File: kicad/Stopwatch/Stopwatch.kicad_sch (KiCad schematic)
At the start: 8 parts

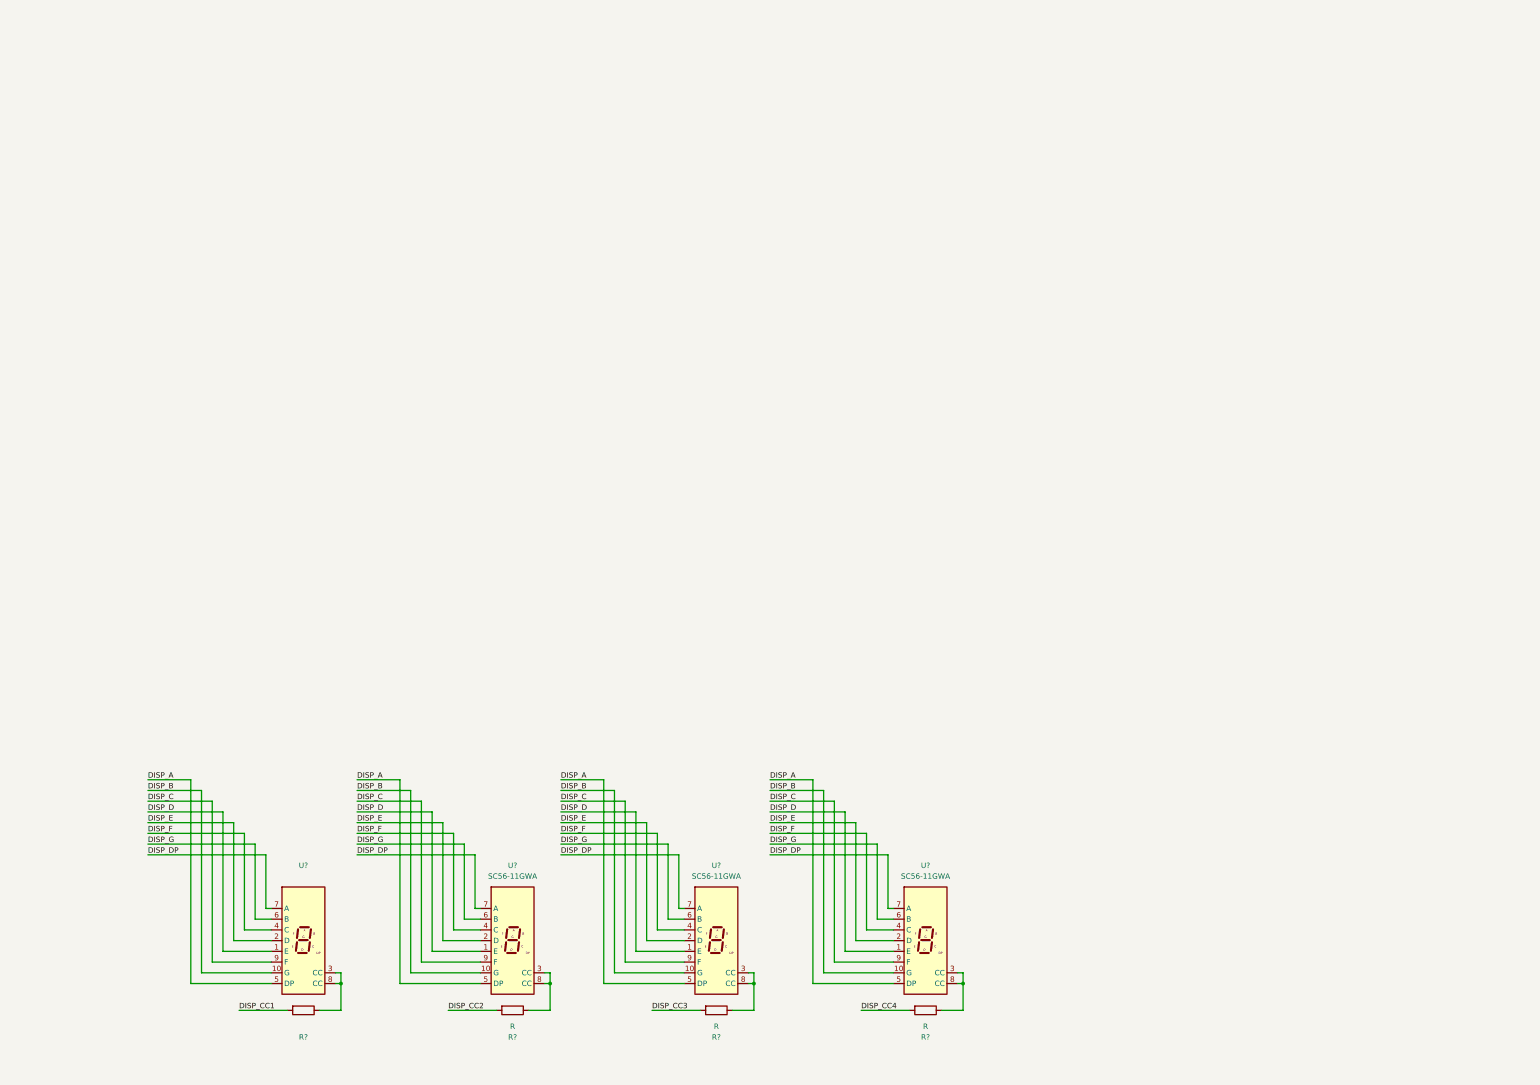
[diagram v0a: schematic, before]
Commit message: added BluePill to symbol library, completed first draft of Stopwatch schematic
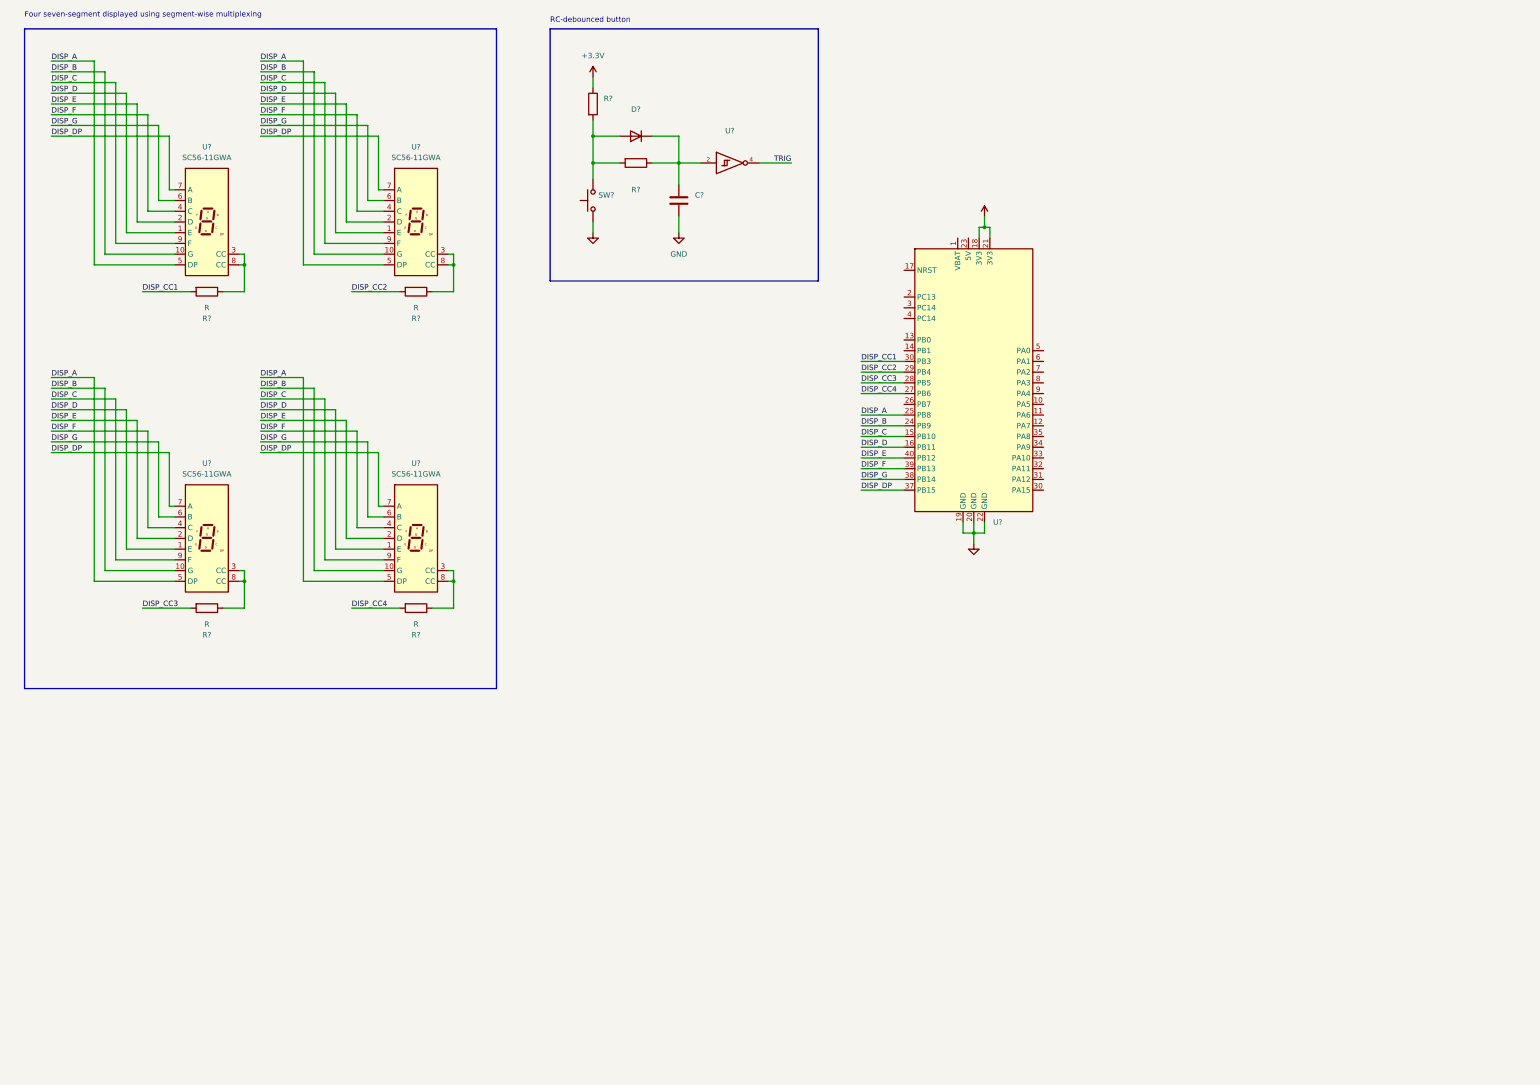
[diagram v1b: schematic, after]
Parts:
- added C?: (no value), symbol Device:C
- added D?: (no value), symbol Diode:1N4148
- added R? (x2): (no value), symbol Device:R
- added SW?: (no value), symbol Switch:SW_Push
- added U?: (no value), symbol 74xGxx:74AHCT1G14
- added U?: (no value), symbol Custom:BluePill
- R?: value (none) -> R
- U?: value (none) -> SC56-11GWA
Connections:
- net DISP_A: now also U?.25 (PB8)
- net DISP_B: now also U?.24 (PB9)
- net DISP_C: now also U?.15 (PB10)
- net DISP_CC1: now also U?.30 (PB3)
- net DISP_CC2: now also U?.29 (PB4)
- net DISP_CC3: now also U?.28 (PB5)
- net DISP_CC4: now also U?.27 (PB6)
- net DISP_D: now also U?.16 (PB11)
- net DISP_DP: now also U?.37 (PB15)
- net DISP_E: now also U?.40 (PB12)
- net DISP_F: now also U?.39 (PB13)
- net DISP_G: now also U?.38 (PB14)
- new net: C?.1, D?.1 (K), R?.1, U?.2
- new net: D?.2 (A), R?.2, R?.2, SW?.2
- new net +3V3: R?.1, U?.18 (3V3), U?.21 (3V3)
- new net GND: C?.2, SW?.1, U?.19 (GND), U?.20 (GND), U?.22 (GND), U?.3 (GND)
- new net TRIG: U?.4
- new net VCC: U?.5 (VCC)
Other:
- note added: "Four seven-segment displayed using segment-wise multiplexing"
- note added: "RC-debounced button"
- moved on the sheet: R?, U?

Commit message: updated Stopwatch with calculation for debouncer circuit
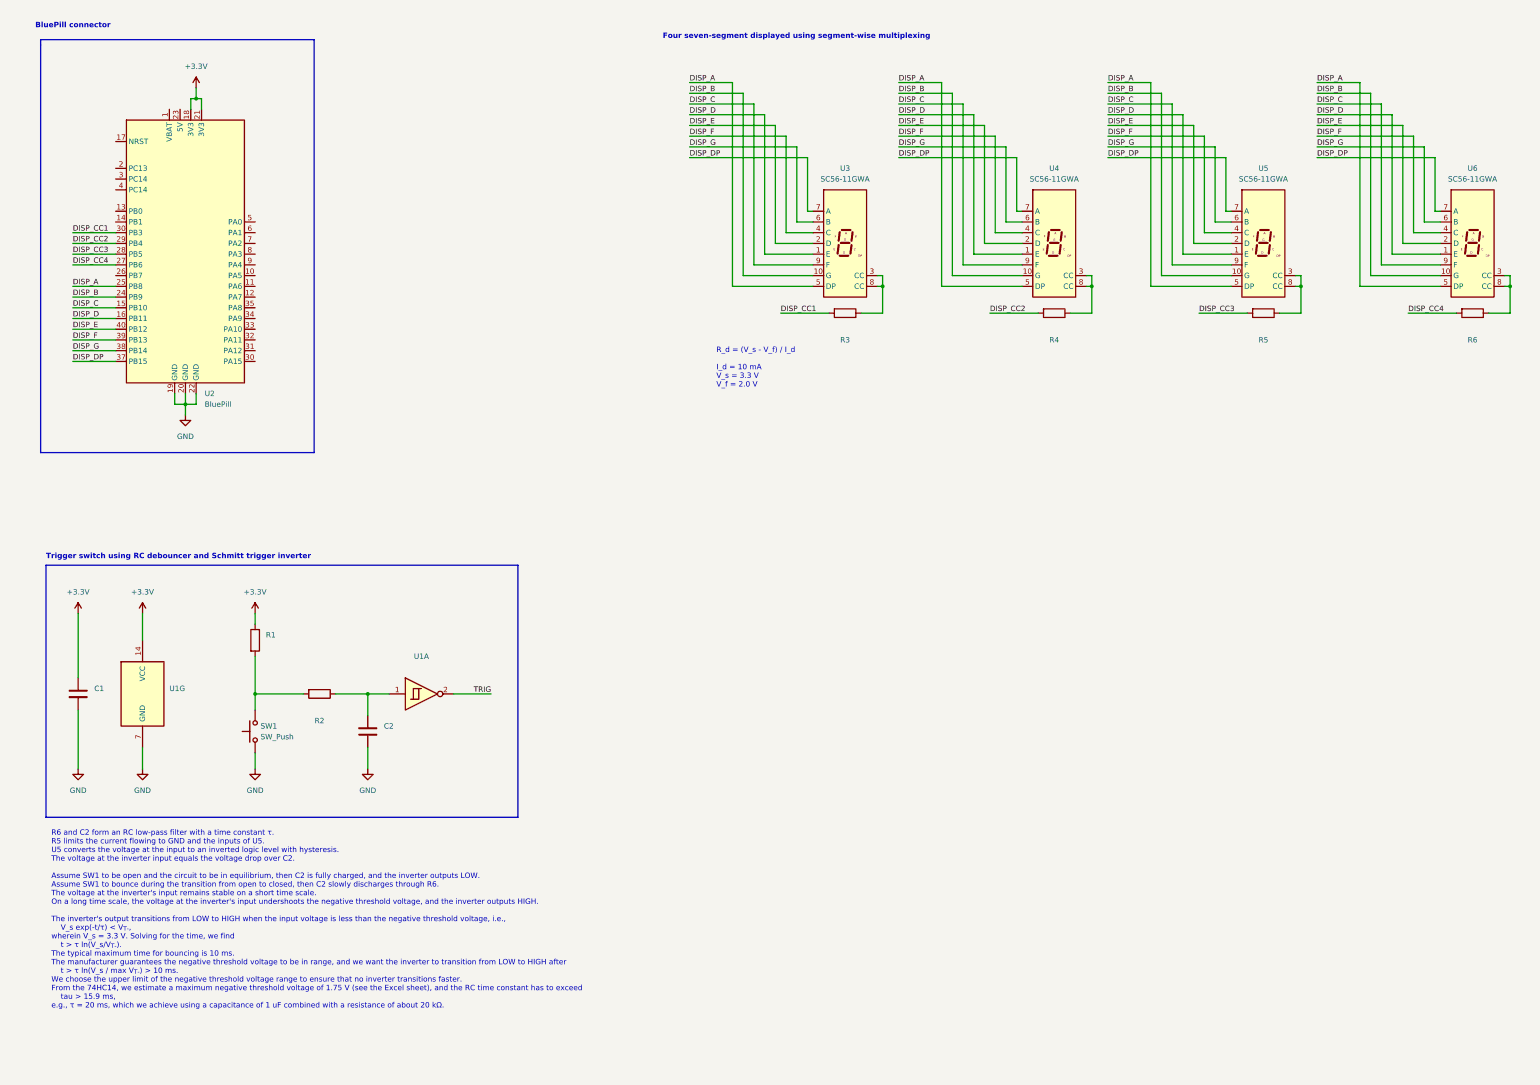
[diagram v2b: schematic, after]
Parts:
- removed D?: (no value), symbol Diode:1N4148
- removed U?: (no value), symbol 74xGxx:74AHCT1G14
- added C1: (no value), symbol Device:C
- added U1: (no value), symbol 74xx:74HC14
- R3, R4, R5, R6: renamed from R?; value R -> (none)
- SW1: renamed from SW?; value (none) -> SW_Push
- U2: renamed from U?; value (none) -> BluePill
- gave numbers to parts that had none: 7
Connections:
- net +3V3: now also C1.1, U1.14 (VCC)
- net GND: now also C1.2, U1.7 (GND)
- net TRIG: now also U1.2
- net at C2.1, R2.1: now also U1.1
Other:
- note added: "BluePill connector"
- note added: "R6 and C2 form an RC low-pass filter with a time constant τ. R5 limits the current flowing to GND and the inputs of U5. U5 converts the voltage at the input to an inverted logic level with hysteresis. The voltage at the inverter input equals the voltage drop over C2. Assume SW1 to be open and the circuit to be in equilibrium, then C2 is fully charged, and the inverter outputs LOW. Assume SW1 to b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"
- note added: "R_d = (V_s - V_f) / I_d I_d = 10 mA V_s = 3.3 V V_f = 2.0 V"
- note added: "Trigger switch using RC debouncer and Schmitt trigger inverter"
- note removed: "RC-debounced button"
- company: (none) -> Bodo Kaiser
- title: (none) -> BluePill Stopwatch
- moved on the sheet: C2, R1, R2, R3, R4, R5, R6, SW1, U2, U3, U4, U5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

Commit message: fixed custom BluePill symbol and updated Stopwatch schematic
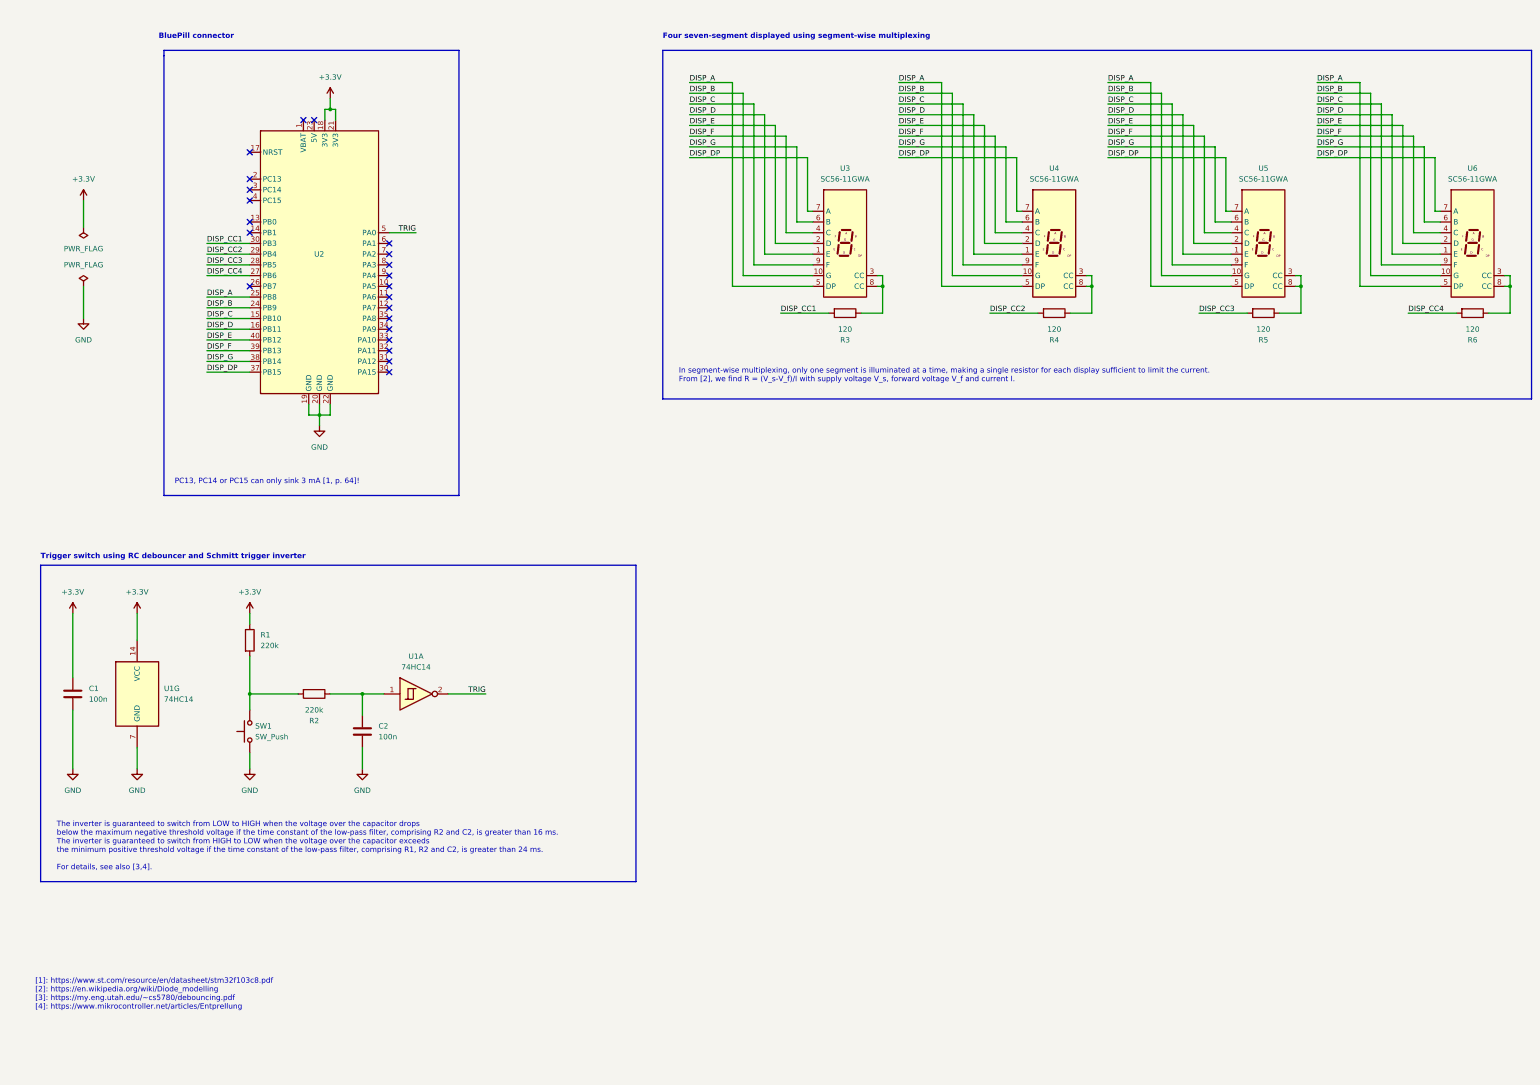
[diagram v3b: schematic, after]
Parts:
- C1, C2: value (none) -> 100n
- R1, R2: value (none) -> 220k
- R3, R4, R5, R6: value (none) -> 120
- U1: value (none) -> 74HC14
- U2: value BluePill -> (none)
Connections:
- net TRIG: now also U2.5 (PA0)
- no-connect marks 0 -> 22
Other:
- note added: "In segment-wise multiplexing, only one segment is illuminated at a time, making a single resistor for each display sufficient to limit the current. From [2], we find R = (V_s-V_f)/I with supply voltage V_s, forward voltage V_f and current I."
- note added: "PC13, PC14 or PC15 can only sink 3 mA [1, p. 64]!"
- note added: "The inverter is guaranteed to switch from LOW to HIGH when the voltage over the capacitor drops below the maximum negative threshold voltage if the time constant of the low-pass filter, comprising R2 and C2, is greater than 16 ms. The inverter is guaranteed to switch from HIGH to LOW when the voltage over the capacitor exceeds the minimum positive threshold voltage if the time constant of the low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"
- note added: "[1]: https://www.st.com/resource/en/datasheet/stm32f103c8.pdf [2]: https://en.wikipedia.org/wiki/Diode_modelling [3]: https://my.eng.utah.edu/~cs5780/debouncing.pdf [4]: https://www.mikrocontroller.net/articles/Entprellung"
- note removed: "R6 and C2 form an RC low-pass filter with a time constant τ. R5 limits the current flowing to GND and the inputs of U5. U5 converts the voltage at the input to an inverted logic level with hysteresis. The voltage at the inverter input equals the voltage drop over C2. Assume SW1 to be open and the circuit to be in equilibrium, then C2 is fully charged, and the inverter outputs LOW. Assume SW1 to b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"
- note removed: "R_d = (V_s - V_f) / I_d I_d = 10 mA V_s = 3.3 V V_f = 2.0 V"
- moved on the sheet: C1, C2, R1, R2, SW1, U1A, U1G, U2

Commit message: added custom footprint library with SC56-11GWA, assigned available footprints
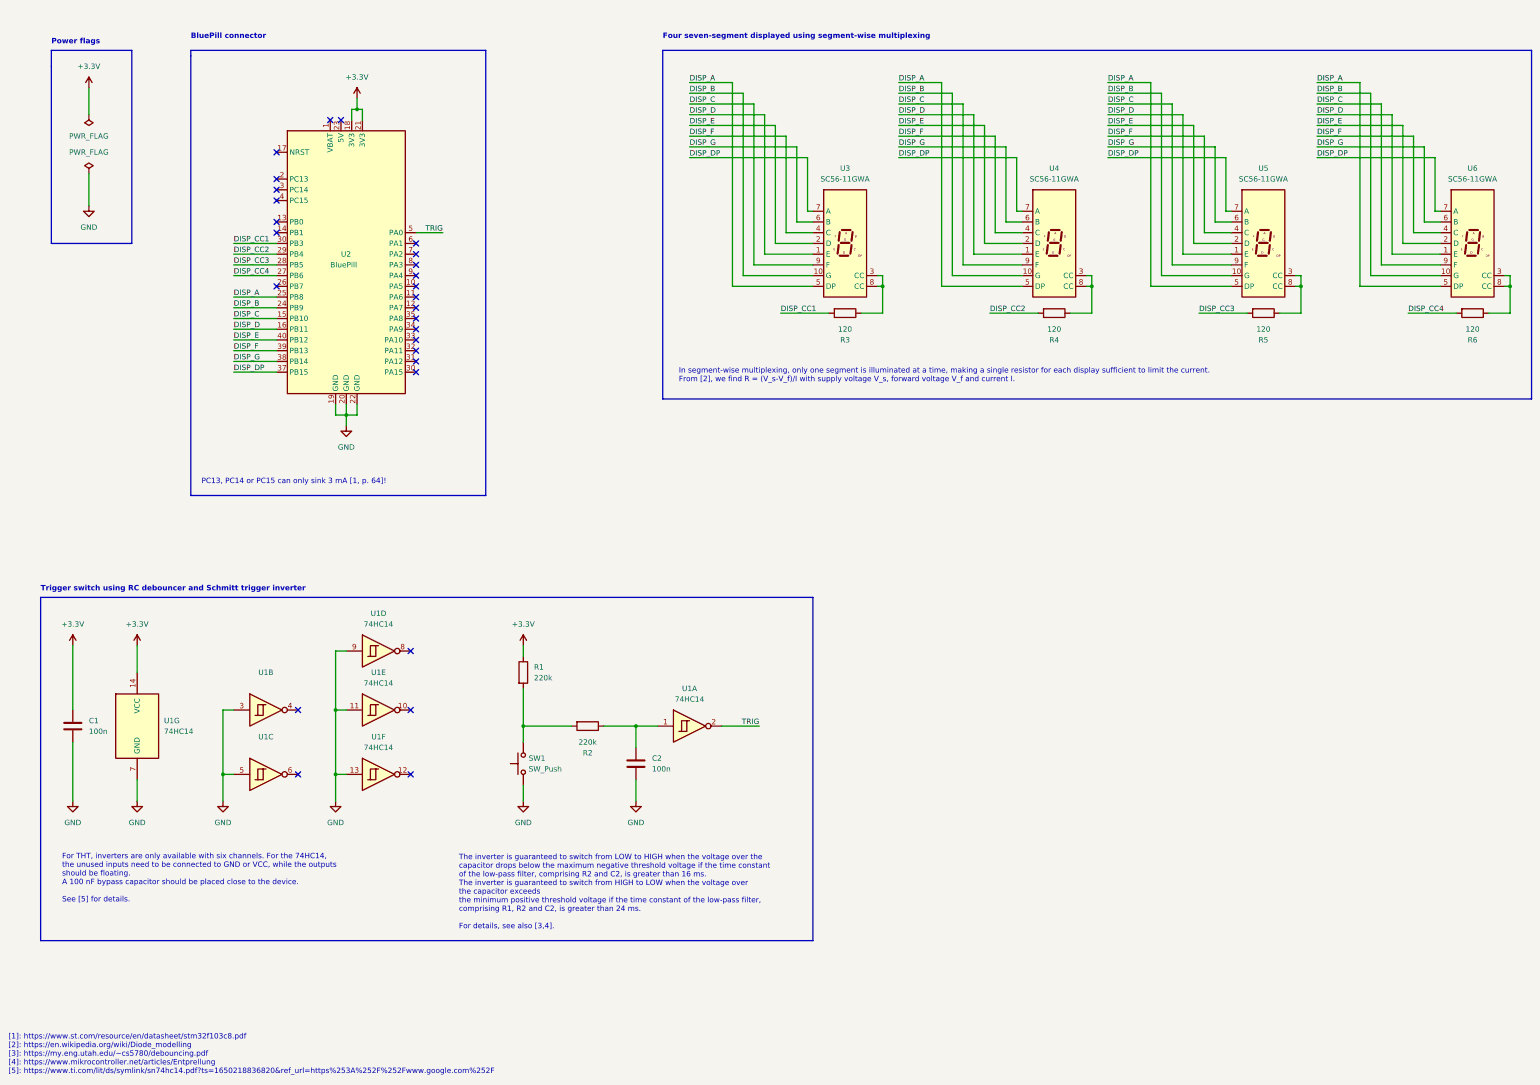
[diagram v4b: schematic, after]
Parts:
- added unit 4 of U1
- added unit 3 of U1
- added unit 5 of U1
- added unit 2 of U1
- added unit 6 of U1
- U2: value (none) -> BluePill
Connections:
- net GND: now also U1.11, U1.13, U1.3, U1.5, U1.9
- no-connect marks 22 -> 27
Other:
- note added: "For THT, inverters are only available with six channels. For the 74HC14, the unused inputs need to be connected to GND or VCC, while the outputs should be floating. A 100 nF bypass capacitor should be placed close to the device. See [5] for details."
- note added: "Power flags"
- note added: "[1]: https://www.st.com/resource/en/datasheet/stm32f103c8.pdf [2]: https://en.wikipedia.org/wiki/Diode_modelling [3]: https://my.eng.utah.edu/~cs5780/debouncing.pdf [4]: https://www.mikrocontroller.net/articles/Entprellung [5]: https://www.ti.com/lit/ds/symlink/sn74hc14.pdf?ts=1650218836820&ref_url=https%253A%252F%252Fwww.google.com%252F"
- note removed: "[1]: https://www.st.com/resource/en/datasheet/stm32f103c8.pdf [2]: https://en.wikipedia.org/wiki/Diode_modelling [3]: https://my.eng.utah.edu/~cs5780/debouncing.pdf [4]: https://www.mikrocontroller.net/articles/Entprellung"
- moved on the sheet: C1, C2, R1, R2, SW1, U1A, U1G, U2
